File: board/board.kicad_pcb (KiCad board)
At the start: 2 copper layers, 20.3 x 20.3 mm, 4 parts, among them U1 ATtiny13A-PU, U2 E07-M1101D, U3 DFR0579

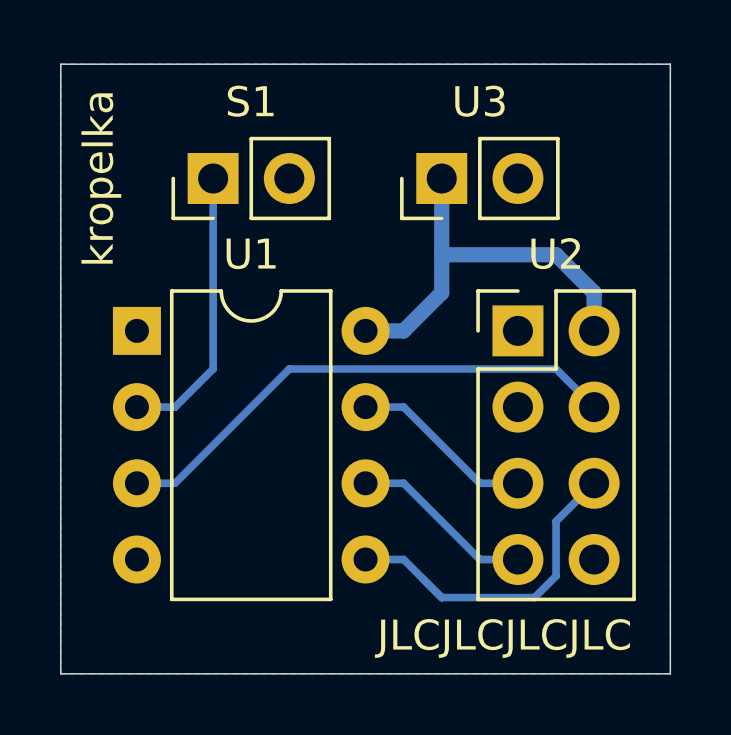
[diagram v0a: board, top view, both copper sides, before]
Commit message: Add silkscreen +/- markings
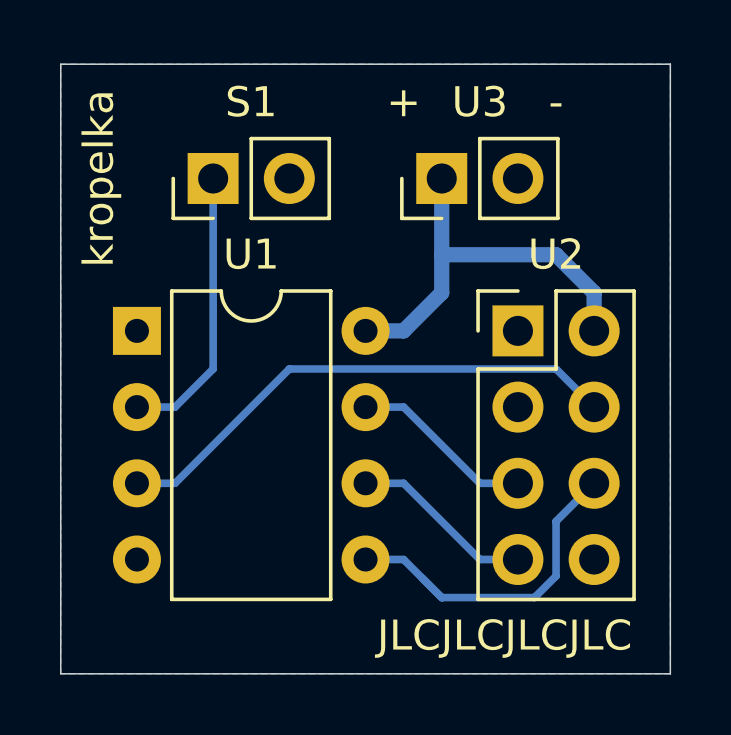
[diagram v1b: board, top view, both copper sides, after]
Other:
- board text added: "+"
- board text added: "-"
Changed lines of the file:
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@@
   (general
     (thickness 1.6)
-    (drawings 6)
+    (drawings 8)
     (tracks 27)
     (zones 0)
@@
     )
   )
+  (gr_text - (at 123.19 97.79) (layer F.SilkS)
+    (effects (font (size 1 1) (thickness 0.15)))
+  )
+  (gr_text + (at 118.11 97.79) (layer F.SilkS)
+    (effects (font (size 1 1) (thickness 0.15)))
+  )
   (gr_text kropelka (at 107.95 100.33 90) (layer F.SilkS)
